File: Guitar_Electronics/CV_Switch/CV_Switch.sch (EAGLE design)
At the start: 7 parts

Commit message: Licenses
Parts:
- added C2: 10uF, resistor:C-EUC0805
- C1: value 0.1uF -> 10uF
- U$1: value 5WAY_SW_1_ -> 5WAY_SW_1; device CYCFI_switch:5WAY_SW_1_ -> CYCFI_switch:5WAY_SW_1
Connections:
- net GND: now also C2.2
- net N$1: now also C2.1
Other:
- note added: "CV Switch for Nexus Project by Cycfi Research is licensed under a Creative Commons Attribution-ShareAlike 4.0 International License. Copyright CYCFI Research Inc. 2013-2016"
- note removed: "Nexus Project by Cycfi Research is licensed under a Creative Commons Attribution-NonCommercial 4.0 International License. http://creativecommons.org/licenses/by-nc/4.0/ Copyright CYCFI Research Inc. 2013-2016"
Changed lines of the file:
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@@
 <part name="SUPPLY2" library="supply2" deviceset="GND" device=""/>
 <part name="SUPPLY3" library="supply2" deviceset="GND" device=""/>
-<part name="U$1" library="CYCFI_switch" deviceset="5WAY_SW_1" device="_"/>
-<part name="C1" library="resistor" deviceset="C-EU" device="C0805" value="0.1uF"/>
+<part name="U$1" library="CYCFI_switch" deviceset="5WAY_SW_1" device="" value="5WAY_SW_1"/>
+<part name="C1" library="resistor" deviceset="C-EU" device="C0805" value="10uF"/>
 <part name="SUPPLY4" library="supply2" deviceset="GND" device=""/>
+<part name="C2" library="resistor" deviceset="C-EU" device="C0805" value="10uF"/>
 </parts>
 <sheets>
@@
 <text x="168.275" y="17.78" size="2.54" layer="95">5Way Switch - Control Voltage</text>
 <text x="238.125" y="6.985" size="2.1844" layer="95">v0.92</text>
-<text x="10.16" y="7.62" size="2.54" layer="95">Nexus Project by Cycfi Research is licensed under a
-Creative Commons Attribution-NonCommercial 4.0
-International License.
-http://creativecommons.org/licenses/by-nc/4.0/
+<text x="10.16" y="7.62" size="2.54" layer="95">CV Switch for Nexus Project by Cycfi Research is licensed under a
+Creative Commons Attribution-ShareAlike 4.0 International License.
 Copyright CYCFI Research Inc. 2013-2016</text>
 <text x="111.76" y="64.77" size="1.778" layer="95">POSITION</text>
@@
 <instance part="C1" gate="G$1" x="159.385" y="92.71"/>
 <instance part="SUPPLY4" gate="GND" x="159.385" y="80.645"/>
+<instance part="C2" gate="G$1" x="151.765" y="128.905"/>
 </instances>
 <busses>
@@
 <pinref part="H1" gate="G$1" pin="3"/>
 <pinref part="R1" gate="G$1" pin="2"/>
-<wire x1="165.735" y1="133.985" x2="78.105" y2="133.985" width="0.1524" layer="91"/>
+<wire x1="165.735" y1="133.985" x2="151.765" y2="133.985" width="0.1524" layer="91"/>
+<pinref part="C2" gate="G$1" pin="1"/>
+<wire x1="151.765" y1="133.985" x2="78.105" y2="133.985" width="0.1524" layer="91"/>
+<wire x1="151.765" y1="131.445" x2="151.765" y2="133.985" width="0.1524" layer="91"/>
+<junction x="151.765" y="133.985"/>
 </segment>
 </net>
@@
 <wire x1="165.735" y1="136.525" x2="161.925" y2="136.525" width="0.1524" layer="91"/>
 <wire x1="161.925" y1="136.525" x2="161.925" y2="121.285" width="0.1524" layer="91"/>
-</segment>
-<segment>
+<pinref part="C2" gate="G$1" pin="2"/>
+<wire x1="151.765" y1="123.825" x2="151.765" y2="121.285" width="0.1524" layer="91"/>
+<wire x1="151.765" y1="121.285" x2="161.925" y2="121.285" width="0.1524" layer="91"/>
+<junction x="161.925" y="121.285"/>
+</segment>
+<segment>

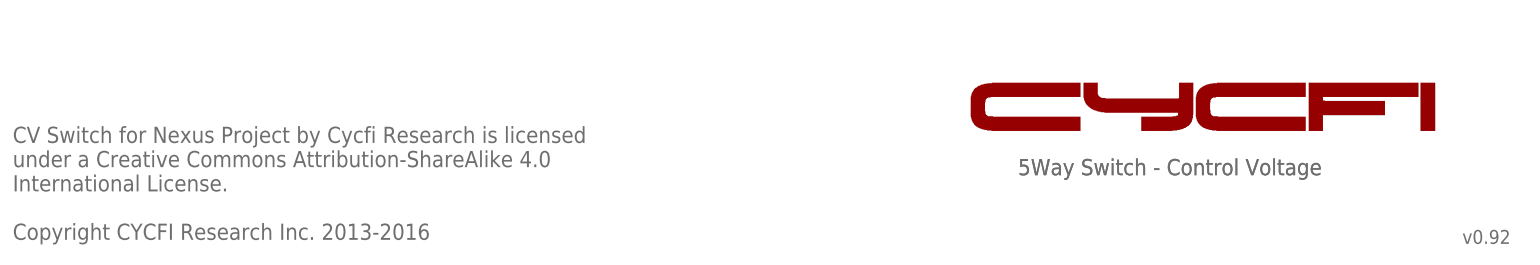
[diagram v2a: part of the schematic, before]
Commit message: Updated copyright and document number of schematics
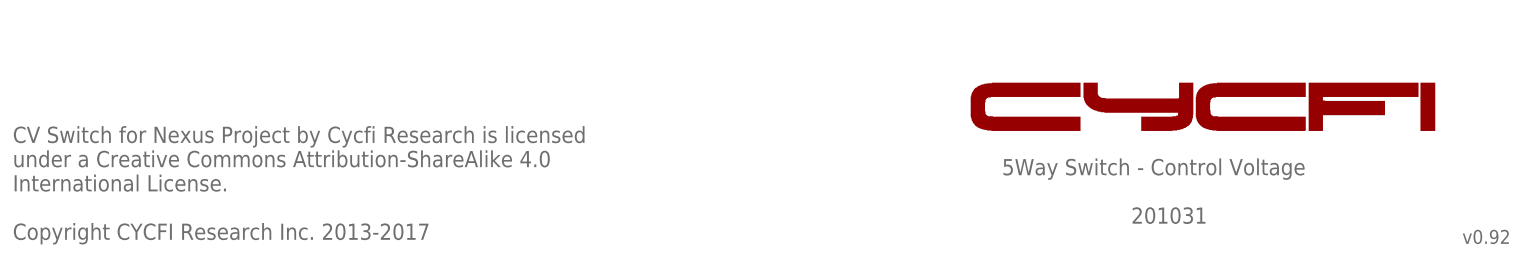
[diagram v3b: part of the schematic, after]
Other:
- note added: "201031"
- note added: "CV Switch for Nexus Project by Cycfi Research is licensed under a Creative Commons Attribution-ShareAlike 4.0 International License. Copyright CYCFI Research Inc. 2013-2017"
- note removed: "CV Switch for Nexus Project by Cycfi Research is licensed under a Creative Commons Attribution-ShareAlike 4.0 International License. Copyright CYCFI Research Inc. 2013-2016"
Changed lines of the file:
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@@
 <?xml version="1.0" encoding="utf-8"?>
 <!DOCTYPE eagle SYSTEM "eagle.dtd">
-<eagle version="6.3">
+<eagle version="7.6.0">
 <drawing>
 <settings>
@@
 <text x="180.34" y="137.16" size="1.778" layer="95" rot="R180">GND</text>
 <text x="180.34" y="139.7" size="1.778" layer="95" rot="R180">OUT</text>
-<text x="168.275" y="17.78" size="2.54" layer="96">5Way Switch - Control Voltage</text>
-<text x="168.275" y="17.78" size="2.54" layer="95">5Way Switch - Control Voltage</text>
+<text x="165.735" y="17.78" size="2.54" layer="96">5Way Switch - Control Voltage</text>
+<text x="186.055" y="10.16" size="2.54" layer="95">201031</text>
 <text x="238.125" y="6.985" size="2.1844" layer="95">v0.92</text>
 <text x="10.16" y="7.62" size="2.54" layer="95">CV Switch for Nexus Project by Cycfi Research is licensed
 under a Creative Commons Attribution-ShareAlike 4.0
 International License.
-Copyright CYCFI Research Inc. 2013-2016</text>
+Copyright CYCFI Research Inc. 2013-2017</text>
 <text x="111.76" y="64.77" size="1.778" layer="95">POSITION</text>
 <text x="125.73" y="64.77" size="1.778" layer="95">OUTPUT</text>
